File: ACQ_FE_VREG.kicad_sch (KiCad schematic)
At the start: 53 parts, among them U11 NCP161ASN330T1G, U12 NCP161ASN330T1G, U13 LM27761, U14 REF2025, U15 OPA140AIDBVR

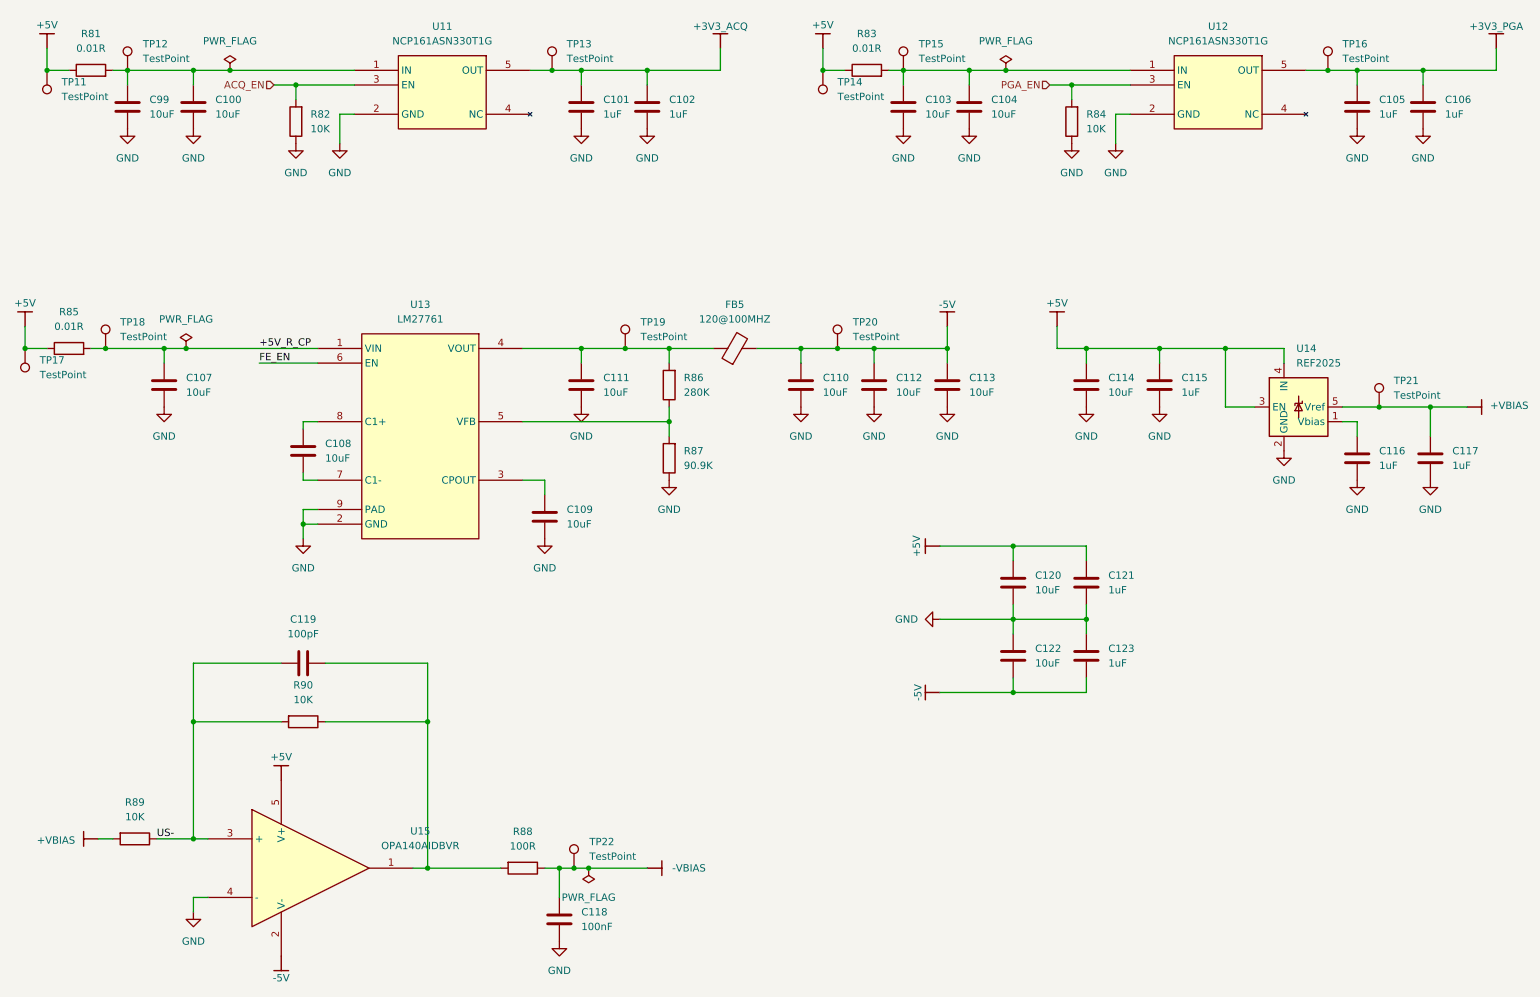
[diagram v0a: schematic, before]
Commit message: added ADC, added FE trim. now all that's left is the micromicrocontroller
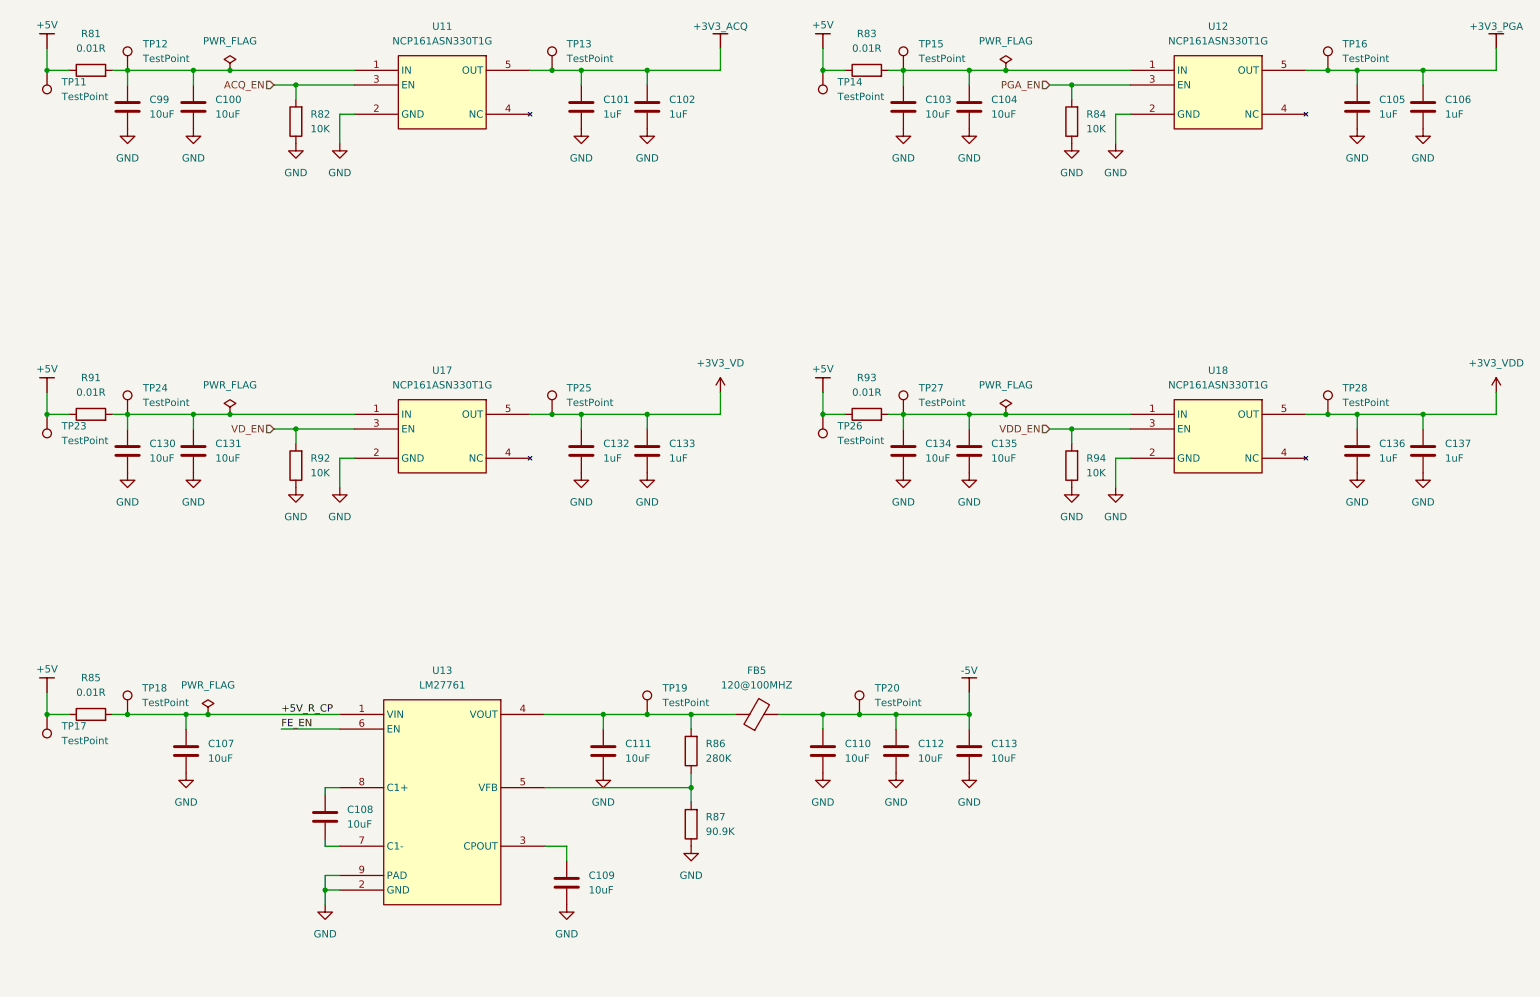
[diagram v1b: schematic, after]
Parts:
- removed C114: 10uF, Capacitor_SMD:C_0402_1005Metric_Pad0.74x0.62mm_HandSolder, symbol Device:C
- removed C115, C116, C117: 1uF, Capacitor_SMD:C_0402_1005Metric_Pad0.74x0.62mm_HandSolder, symbol Device:C
- removed C118: 100nF, Capacitor_SMD:C_0402_1005Metric_Pad0.74x0.62mm_HandSolder, symbol Device:C
- removed C119: 100pF, Capacitor_SMD:C_0402_1005Metric_Pad0.74x0.62mm_HandSolder, symbol Device:C
- removed C120, C122: 10uF, Capacitor_SMD:C_0603_1608Metric_Pad1.08x0.95mm_HandSolder, symbol Device:C
- removed C121, C123: 1uF, Capacitor_SMD:C_0603_1608Metric_Pad1.08x0.95mm_HandSolder, symbol Device:C
- removed R88: 100R, Resistor_SMD:R_0402_1005Metric_Pad0.72x0.64mm_HandSolder, symbol Device:R
- removed R89, R90: 10K, Capacitor_SMD:C_0603_1608Metric_Pad1.08x0.95mm_HandSolder, symbol Device:R
- removed TP21, TP22: TestPoint, TestPoint:TestPoint_Pad_D1.0mm, symbol Connector:TestPoint
- removed U14: REF2025, Package_TO_SOT_SMD:SOT-23-5_HandSoldering, symbol Reference_Voltage:REF2025
- removed U15: OPA140AIDBVR, Thunderscope_Rev5:GEN_SOT23_5_950_2900X1600X1450, symbol Thunderscope_Rev5:IC OPAMP OPA140
- added C130, C131, C134, C135: 10uF, Capacitor_SMD:C_0402_1005Metric_Pad0.74x0.62mm_HandSolder, symbol Device:C
- added C132, C133, C136, C137: 1uF, Capacitor_SMD:C_0402_1005Metric_Pad0.74x0.62mm_HandSolder, symbol Device:C
- added R91, R93: 0.01R, Resistor_SMD:R_0603_1608Metric_Pad0.98x0.95mm_HandSolder, symbol Device:R
- added R92, R94: 10K, Resistor_SMD:R_0402_1005Metric_Pad0.72x0.64mm_HandSolder, symbol Device:R
- added TP23, TP24, TP25, TP26, TP27, TP28: TestPoint, TestPoint:TestPoint_Pad_D1.0mm, symbol Connector:TestPoint
- added U17, U18: NCP161ASN330T1G, Thunderscope_Rev5:GEN_SOT23_5_950_2900X1600X1450, symbol Thunderscope_Rev5:IC LDO NCP161ASN330T1G
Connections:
- net +5V: now also R91.1, R93.1, TP23.1, TP26.1
- net GND: now also C130.2, C131.2, C132.2, C133.2, C134.2, C135.2, C136.2, C137.2, R92.1, R94.1, U17.2 (GND), U18.2 (GND)
- new net: C130.1, C131.1, R91.2, TP24.1, U17.1 (IN)
- new net: C134.1, C135.1, R93.2, TP27.1, U18.1 (IN)
- new net +3V3_VD: C132.1, C133.1, TP25.1, U17.5 (OUT)
- new net +3V3_VDD: C136.1, C137.1, TP28.1, U18.5 (OUT)
- new net VDD_EN: R94.2, U18.3 (EN)
- new net VD_EN: R92.2, U17.3 (EN)
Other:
- moved on the sheet: C107, C108, C109, C110, C111, C112, C113, FB5, R85, R86, R87, TP17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

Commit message: decided on clk source and MCU
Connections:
- net +3V3_PGA renamed PGA

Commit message: schematic complete. no ERC errors
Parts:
- added J5: Conn_01x02_Socket, Connector_AMASS:AMASS_XT30PW-M_1x02_P2.50mm_Horizontal, symbol Connector:Conn_01x02_Socket
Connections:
- net +5V: now also J5.1 (Pin_1)
- net GND: now also J5.2 (Pin_2)
- net PGA renamed +3V3_PGA
